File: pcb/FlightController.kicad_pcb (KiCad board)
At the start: 4 copper layers, 36 x 36 mm, 52 parts, among them P1 3V3, P10 SWDIO, P11 SWCLK, P2 USB_OTG, P3 CONN_02X04, P4 CKD_SANDWICH, P5 CONN_02X10, P6 RESET, P7 BOOT0, P9 5V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

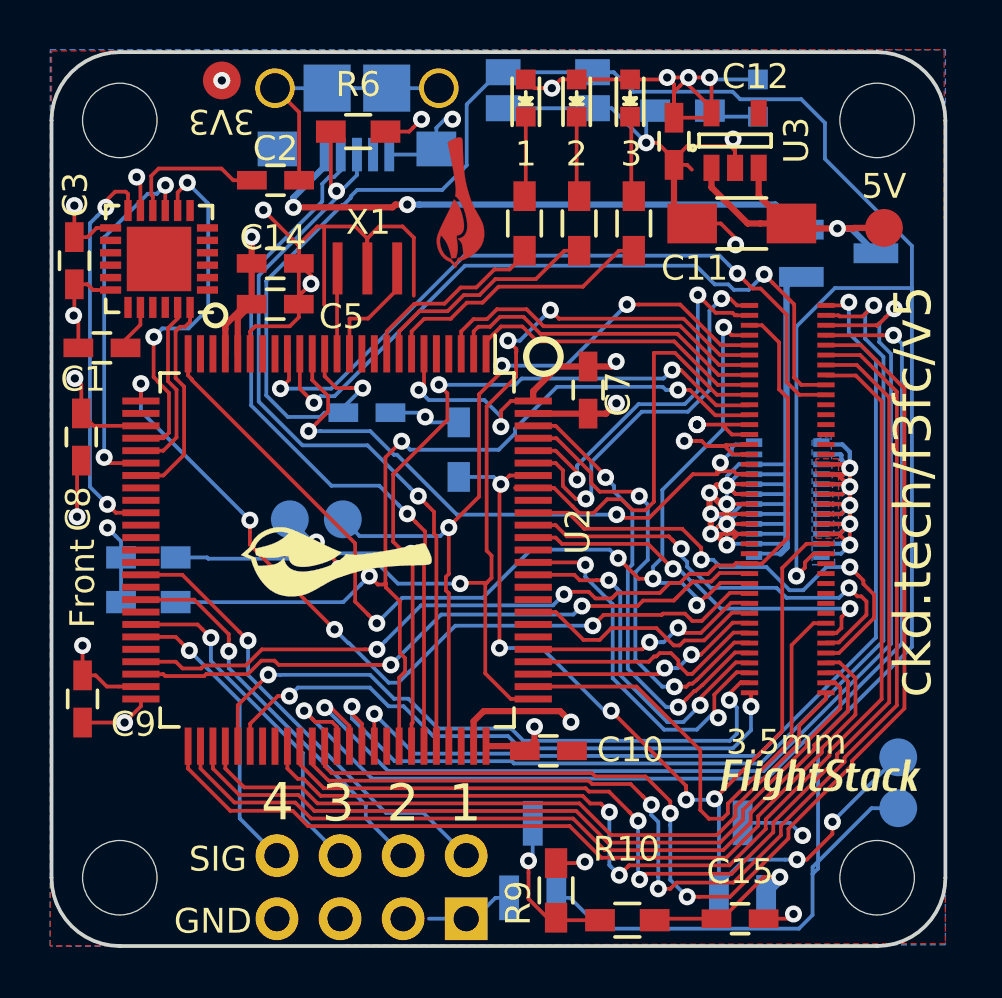
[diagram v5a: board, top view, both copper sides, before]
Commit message: F3FC v6 which features correct reset circuitry.
Also:
* Routes USB as differential pair.
* Corrects reset circuit.
* Adds fiducials
* Matches up LED numbering to reference
* Supports current pin from power connector.
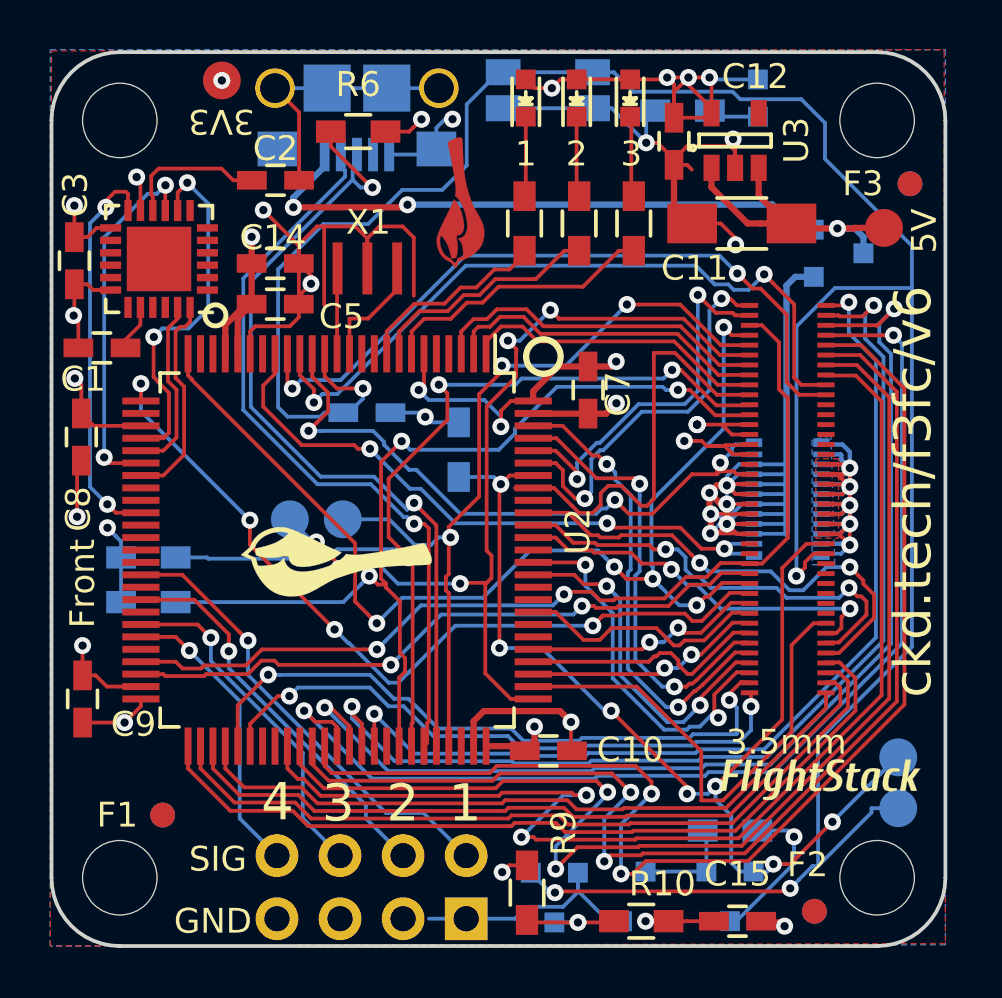
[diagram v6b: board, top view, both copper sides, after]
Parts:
- added F1: 1mm, macrofab:Fiducial, F.Cu at (134.5, 120.7)
- added F2: 1mm, macrofab:Fiducial, F.Cu at (160.7, 124.6)
- added F3: 1mm, macrofab:Fiducial, F.Cu at (164.6, 95.3)
- added F4: 1mm, macrofab:Fiducial, B.Cu at (134.5, 120.7)
- added F5: 1mm, macrofab:Fiducial, B.Cu at (160.7, 124.6)
- added F6: 1mm, macrofab:Fiducial, B.Cu at (164.6, 95.3)
- added Q1: Q_PMOS_GSD, TO_SOT_Packages_SMD:SOT-23, B.Cu at (157.3, 124.0)
- added R7: 10k, Resistors_SMD:R_0603_HandSoldering, B.Cu at (157.3, 121.3)
- D1: renamed from D3; value LED -> Green
- D2: value LED -> Yellow
- D3: renamed from D1; value LED -> Red
- D4, Q3, Q4: footprint Housings_SOT-23_SOT-143_TSOT-6:SOT-23_Handsoldering -> TO_SOT_Packages_SMD:SOT-23
- D5: value PWR -> Red
- moved Q4 4.17 mm to (153.9, 124.0)
- moved Q3 1.73 mm to (150.2, 124.1), turned to 0 degrees
- moved R9 1.17 mm to (149.2, 123.8)
- moved R10 0.56 mm to (153.8, 125.0)
- moved C15 0.14 mm to (157.6, 125.0)
- renumbered R3 to R1, R1 to R3
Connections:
- net /USB_DM renamed /USB_D-
- net /USB_DP renamed /USB_D+
- P5 pad 1: +5V -> /Power/CURRENT
- Q4 pad 2: /Reset/BOOT0 -> GNDPWR
- Q4 pad 3: VDD -> Net-(Q1-Pad1)
- U2 pad 18: Net-(U2-Pad18) -> /Power/CURRENT
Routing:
- net /Power/CURRENT: track 0.00 -> 25.8 mm, vias 0 -> 3
- net GNDPWR: track 132.5 -> 140.2 mm
- net +5V: track 55.9 -> 49.3 mm, vias 7 -> 6
- net Net-(Q1-Pad1): track 0.00 -> 4.16 mm
- net VDD: track 71.4 -> 74.8 mm
- net Net-(C15-Pad1): track 6.81 -> 3.70 mm
- net /TIMG2_CH3: track 45.7 -> 48.5 mm
- net /Reset/BOOT0: track 48.2 -> 45.5 mm
- net /TIMG2_CH4: track 45.8 -> 48.3 mm
- net Net-(Q3-Pad3): track 6.68 -> 4.51 mm
- net /USB_D+: track 32.6 -> 34.4 mm
- net /SPI3_NSS: track 21.1 -> 19.8 mm
- net /Reset/RESET: track 108.5 -> 107.2 mm, vias 2 -> 4
- net /SPI2_NSS: track 34.9 -> 33.7 mm
- net /SPI2_SCK: track 33.2 -> 32.1 mm
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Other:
- net class Default: clearance 0.1524 -> 0.14986
- rule trace_clearance: 0.1524 -> 0.14986
- board text added: "ckd.tech/f3fc/v6"
- board text removed: "ckd.tech/f3fc/v5"

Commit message: More changes to F3. Can't remember what.
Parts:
- removed the G*** at (161.0, 119.3)
- added G***: OSHW, oshw:oshw-4mm, B.Cu at (132.8, 119.7)
- added G***: LOGO, flightstack:flightstack_thin-8mm, F.Cu at (161.0, 119.7)
- added G***: OSHW, oshw:oshw-4mm, F.Cu at (132.8, 119.7)
- added P8: CONN_01X01, Measurement_Points:Measurement_Point_Square-SMD-Pad_Small, B.Cu at (164.6, 97.3)
- moved F6 4.32 mm to (160.3, 95.3)
- moved P6 2.29 mm to (162.4, 118.9)
- moved F4 1.95 mm to (136.4, 120.6)
- moved F1 1.43 mm to (135.9, 120.8)
- moved P7 0.64 mm to (164.6, 118.8)
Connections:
- Q1 pad 2: /Reset/BOOT0 -> VDD
- Q1 pad 3: VDD -> /Reset/BOOT0
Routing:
- net /Reset/RESET: track 107.2 -> 102.1 mm
- net GNDPWR: track 140.2 -> 143.7 mm, vias 21 -> 23
- net /Reset/BOOT0: track 45.5 -> 48.9 mm, vias 7 -> 5
- net VDD: track 74.8 -> 71.9 mm
- net /TIM16_CH1: track 16.1 -> 14.9 mm
- net /UART1_TX: track 18.0 -> 19.0 mm
- net /TIM17_CH1: track 15.4 -> 14.6 mm
- net /UART1_RX: track 18.7 -> 19.5 mm
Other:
- board text added: "G"
- board text added: "ckd.tech/f3fc/v8"
- board text removed: "ckd.tech/f3fc/v6"

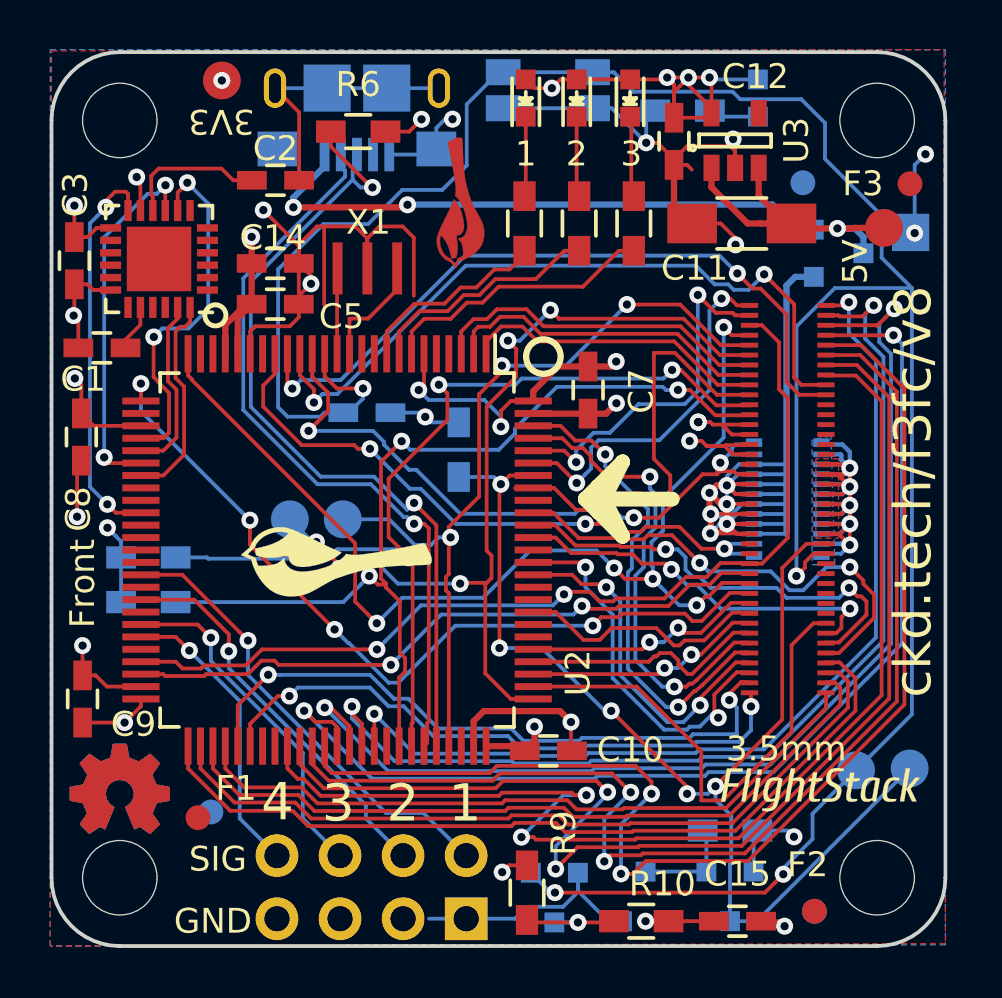
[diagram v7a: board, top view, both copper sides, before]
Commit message: Rebrand everything to Polystack and increment versions.
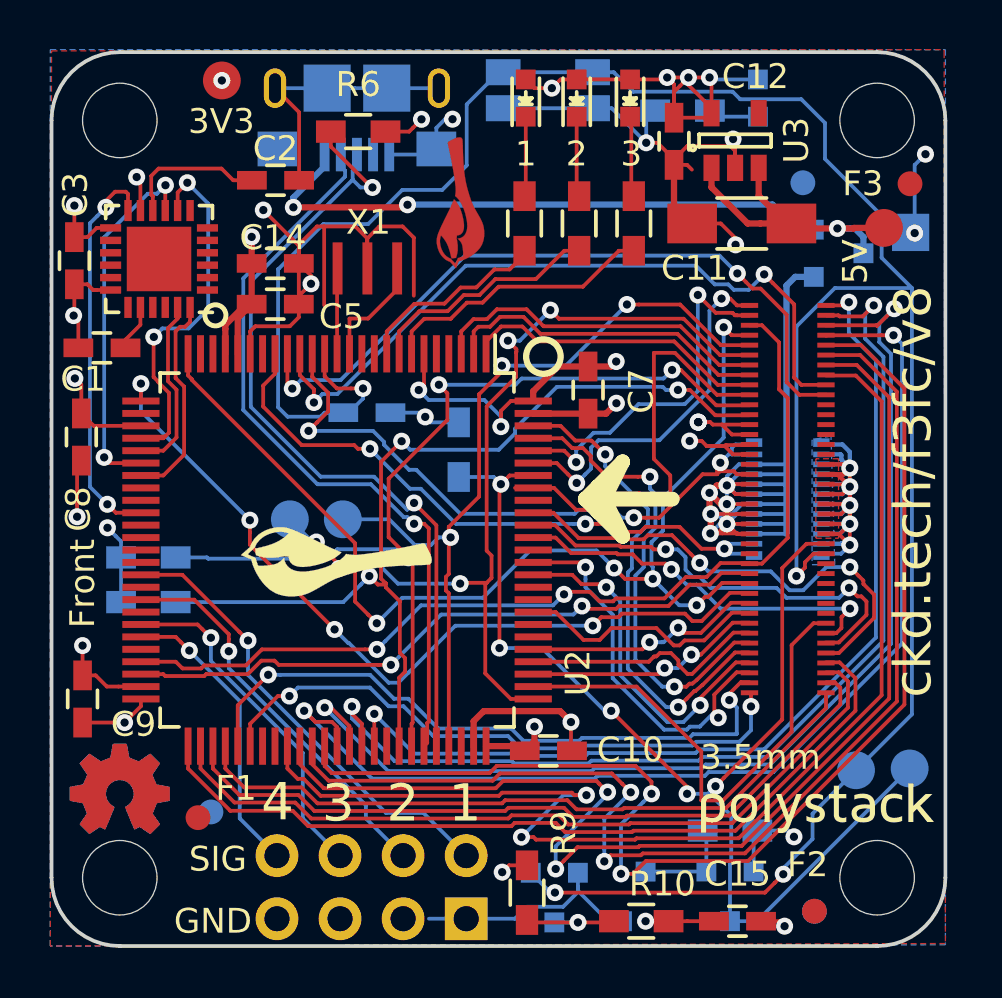
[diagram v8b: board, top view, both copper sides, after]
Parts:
- removed the G*** at (161.0, 119.7)
- added svg2mod: G***, polystack:polystack-medium-10mm, F.Cu at (160.8, 120.5)
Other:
- rule pad_to_mask_clearance: 0.2 -> 0.0762
